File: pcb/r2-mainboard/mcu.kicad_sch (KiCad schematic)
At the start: 28 parts, among them J20 SWD+JTAG (DNP), Q9 AO3400A, SW20 SW, SW21 SW, SW22 SW, U20 STM32G0B1RCT6, Y20 32.768kHz

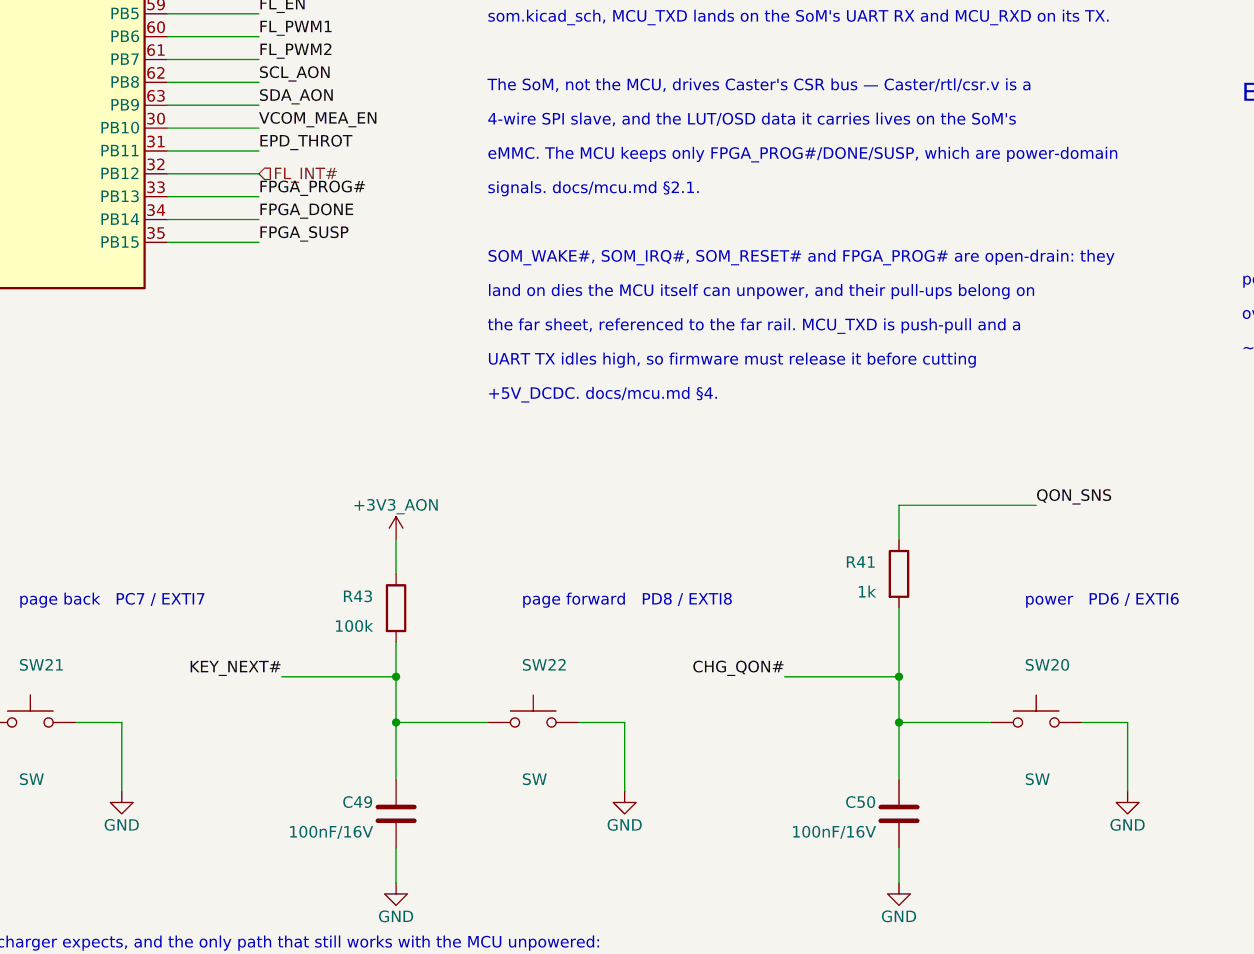
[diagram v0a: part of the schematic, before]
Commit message: routing and board layout
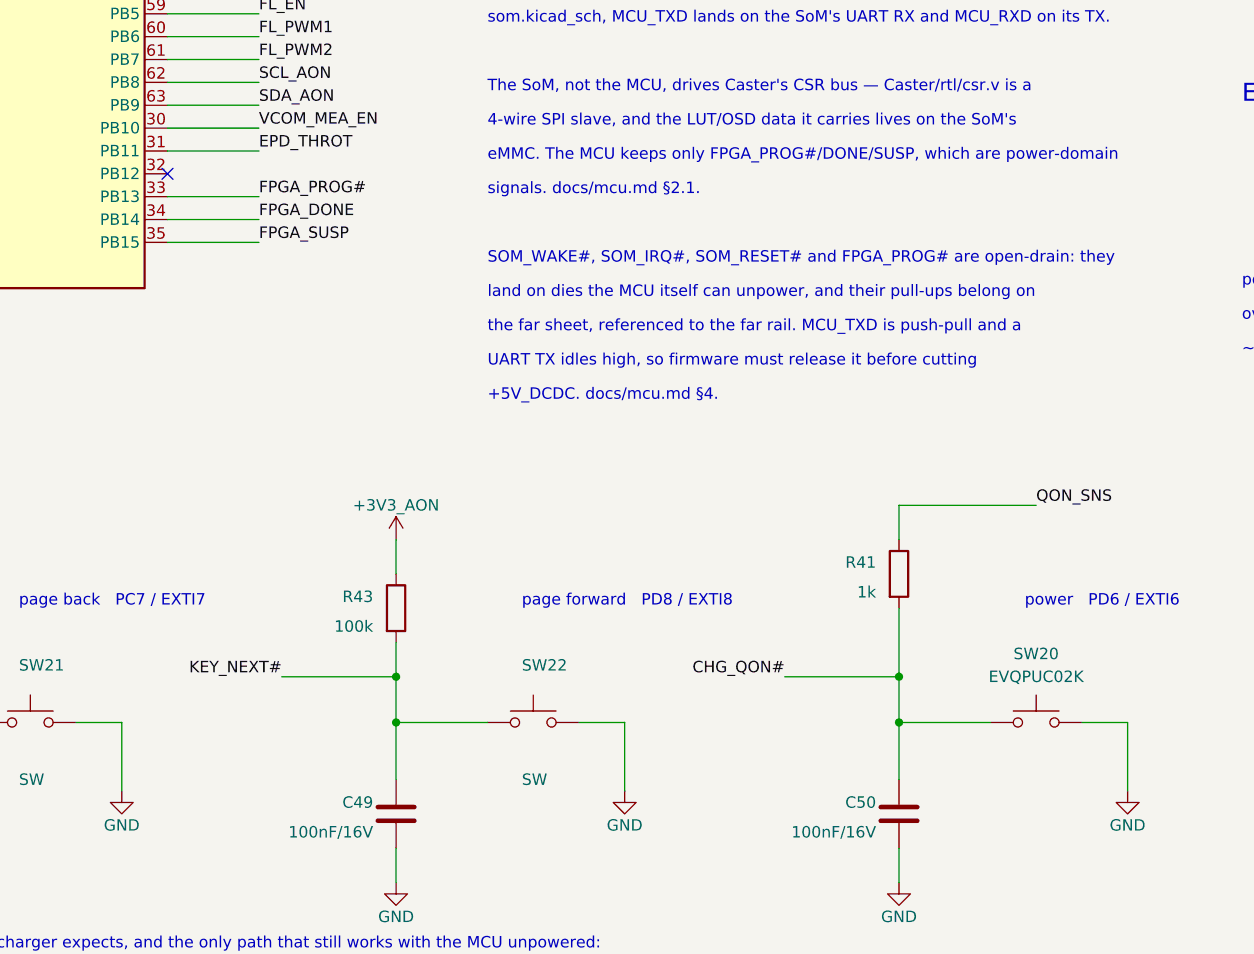
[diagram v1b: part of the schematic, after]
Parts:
- C40: footprint Capacitor_SMD:C_0603_1608Metric -> Capacitor_SMD:C_0402_1005Metric
- SW20: value SW -> EVQPUC02K; footprint Button_Switch_SMD:SW_Push_1P1T_XKB_TS-1187A -> Button_Switch_SMD:Panasonic_EVQPUL_EVQPUC; LCSC C318884 -> (none); MPN TS-1187A-B-A-B -> (none); Manufacturer XKB Connection -> (none)
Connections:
- net FL_INT#: no longer names the net of U20.32 (PB12)
- no-connect marks 1 -> 2
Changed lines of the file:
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@@
 		(at 180.34 139.7)
 	)
+	(no_connect
+		(at 180.34 185.42)
+	)
 	(wire
 		(pts
@@
 	(wire
 		(pts
-			(xy 180.34 185.42) (xy 190.5 185.42)
-		)
-		(stroke
-			(width 0)
-			(type default)
-		)
-	)
-	(wire
-		(pts
 			(xy 220.98 57.15) (xy 228.6 57.15)
 		)
@@
 		)
 	)
-	(hierarchical_label "FL_INT#"
-		(shape input)
-		(at 190.5 185.42 0)
-		(effects
-			(font
-				(size 1.27 1.27)
-			)
-			(justify left)
-		)
-	)
 	(hierarchical_label "SOM_IRQ#"
 		(shape output)
@@
 			)
 		)
-		(property "Footprint" "Capacitor_SMD:C_0603_1608Metric"
+		(property "Footprint" "Capacitor_SMD:C_0402_1005Metric"
 			(at 25.4 49.53 0)
 			(hide yes)
@@
 	)
 	(symbol
-		(lib_id "Switch:SW_Push")
-		(at 276.86 246.38 0)
-		(unit 1)
-		(body_style 1)
-		(exclude_from_sim no)
-		(in_bom yes)
-		(on_board yes)
-		(in_pos_files yes)
-		(dnp no)
-		(property "Reference" "SW20"
-			(at 275.59 240.03 0)
-			(show_name no)
-			(do_not_autoplace no)
-			(effects
-				(font
-					(size 1.27 1.27)
-				)
-				(justify left)
-			)
-		)
-		(property "Value" "SW"
-			(at 275.59 252.73 0)
-			(show_name no)
-			(do_not_autoplace no)
-			(effects
-				(font
-					(size 1.27 1.27)
-				)
-				(justify left)
-			)
-		)
-		(property "Footprint" "Button_Switch_SMD:SW_Push_1P1T_XKB_TS-1187A"
-			(at 276.86 246.38 0)
-			(hide yes)
-			(show_name no)
-			(do_not_autoplace no)
-			(effects
-				(font
-					(size 1.27 1.27)
-				)
-			)
-		)
-		(property "Datasheet" ""
-			(at 276.86 246.38 0)
-			(hide yes)
-			(show_name no)
-			(do_not_autoplace no)
-			(effects
-				(font
-					(size 1.27 1.27)
-				)
-			)
-		)
-		(property "Description" "Power button — shorts CHG_QON# to GND galvanically, the only ship-mode exit needing neither a cable nor a live I²C host (bq25890.pdf §9.2.10.2). 1.6 N, 100 k cycles is ample for a rarely-pressed key (XKB TS-1187A-B-A-B, LCSC C318884, JLC Basic)"
-			(at 276.86 246.38 0)
-			(hide yes)
-			(show_name no)
-			(do_not_autoplace no)
-			(effects
-				(font
-					(size 1.27 1.27)
-				)
-			)
-		)
-		(property "LCSC" "C318884"
-			(at 276.86 246.38 0)
-			(hide yes)
-			(show_name no)
-			(do_not_autoplace no)
-			(effects
-				(font
-					(size 1.27 1.27)
-				)
-			)
-		)
-		(property "Manufacturer" "XKB Connection"
-			(at 0 0 0)
-			(hide yes)
-			(show_name no)
-			(do_not_autoplace no)
-			(effects
-				(font
-					(size 1.27 1.27)
-				)
-			)
-		)
-		(property "MPN" "TS-1187A-B-A-B"
-			(at 0 0 0)
-			(hide yes)
-			(show_name no)
-			(do_not_autoplace no)
-			(effects
-				(font
-					(size 1.27 1.27)
-				)
-			)
-		)
-		(pin "1"
-		)
-		(pin "2"
-		)
-		(instances
-			(project "r2"
-				(path "/dee825bf-c2f1-415d-afdf-cf702072a6e8/a89f58f8-b115-4f71-9806-30f9bff6e587"
-					(reference "SW20")
-					(unit 1)
-				)
-			)
-		)
-	)
-	(symbol
 		(lib_id "Device:R")
 		(at 261.62 229.87 0)
@@
 					(unit 1)
 				)
+			)
+		)
+	)
+	(symbol
+		(lib_id "Switch:SW_Push")
+		(at 276.86 246.38 0)
+		(unit 1)
+		(body_style 1)
+		(exclude_from_sim no)
+		(in_bom yes)
+		(on_board yes)
+		(in_pos_files yes)
+		(dnp no)
+		(fields_autoplaced yes)
+		(property "Reference" "SW20"
+			(at 276.86 238.76 0)
+			(show_name no)
+			(do_not_autoplace no)
+			(effects
+				(font
+					(size 1.27 1.27)
+				)
+			)
+		)
+		(property "Value" "EVQPUC02K"
+			(at 276.86 241.3 0)
+			(show_name no)
+			(do_not_autoplace no)
+			(effects
+				(font
+					(size 1.27 1.27)
+				)
+			)
+		)
+		(property "Footprint" "Button_Switch_SMD:Panasonic_EVQPUL_EVQPUC"
+			(at 276.86 241.3 0)
+			(hide yes)
+			(show_name no)
+			(do_not_autoplace no)
+			(effects
+				(font
+					(size 1.27 1.27)
+				)
+			)
+		)
+		(property "Datasheet" "https://www.lcsc.com/datasheet/C79174.pdf?spm=wm.sxq.inf.ggs___wm.fly.bg.22.stp&lcsc_vid=RFINUQVSFFNZAQFeRFJdBlwHElhYUlNVEwVYVwdTQFgxVlNeQFVdU1deQVBXUjsOAxUeFF5JWBILBhYFH08MFQUQEk8NCAlJ"
+			(at 276.86 241.3 0)
+			(hide yes)
+			(show_name no)
+			(do_not_autoplace no)
+			(effects
+				(font
+					(size 1.27 1.27)
+				)
+			)
+		)
+		(property "Description" "Push button switch, generic, two pins"
+			(at 276.86 246.38 0)
+			(hide yes)
+			(show_name no)
+			(do_not_autoplace no)
+			(effects
+				(font
+					(size 1.27 1.27)
+				)
+			)
+		)
+		(pin "2"
+		)
+		(pin "1"
+		)
+		(instances
+			(project "r2"
+				(path "/dee825bf-c2f1-415d-afdf-cf702072a6e8/a89f58f8-b115-4f71-9806-30f9bff6e587"
+					(reference "SW20")
+					(unit 1)
+				)

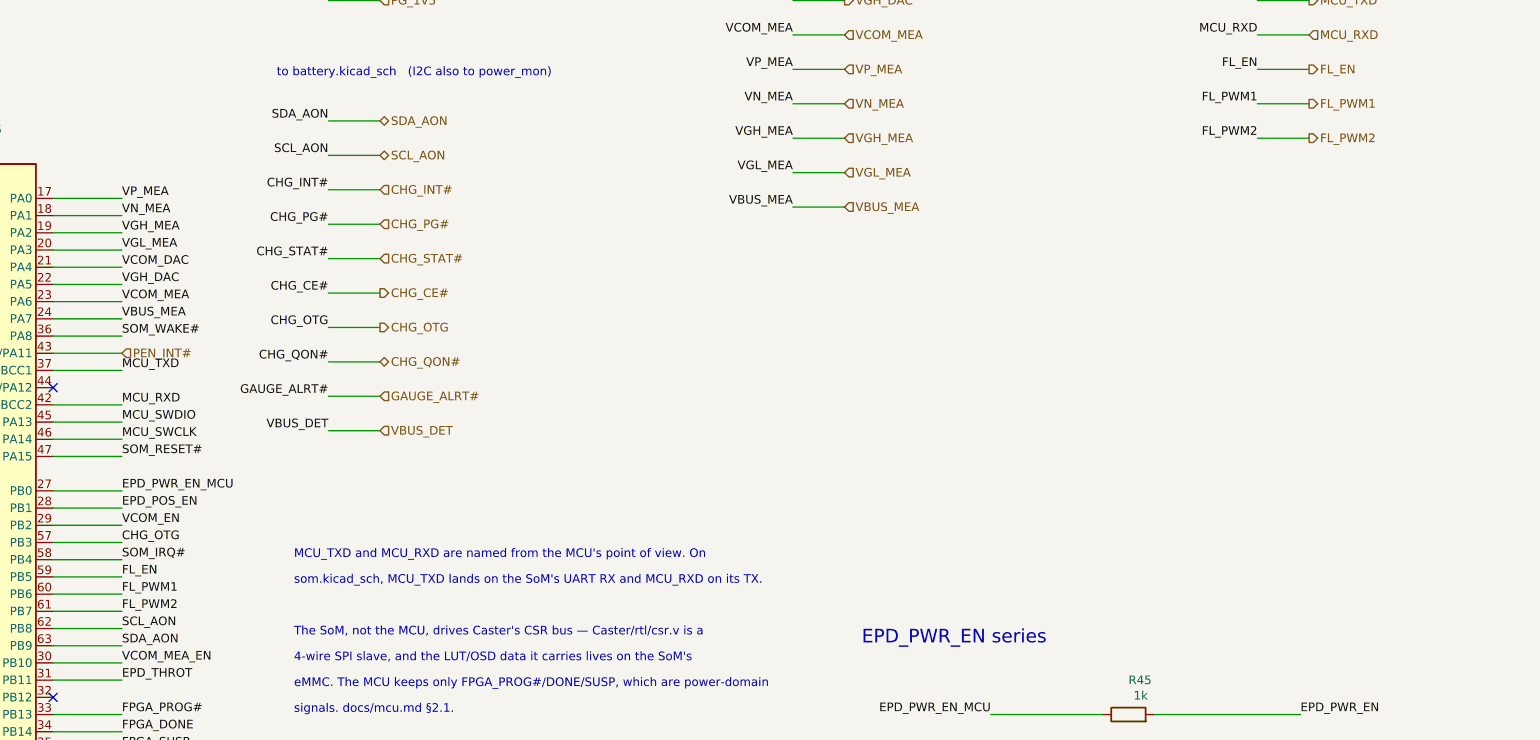
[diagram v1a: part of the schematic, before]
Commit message: change layout and reduce board size + add second usb host only
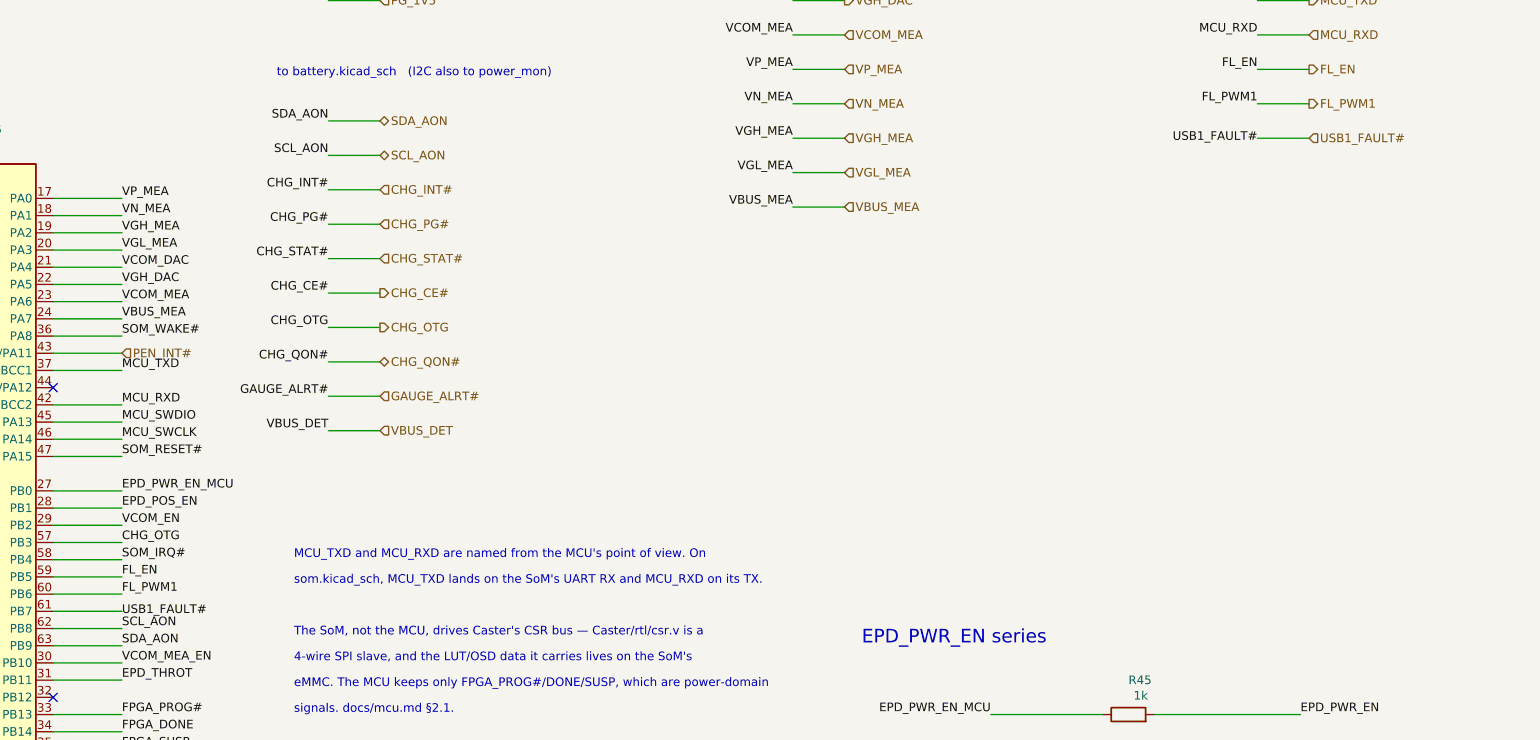
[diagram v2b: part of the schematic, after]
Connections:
- net FL_PWM2 renamed USB1_FAULT#
